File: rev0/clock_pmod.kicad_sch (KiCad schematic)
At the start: 5 parts, among them IC1 ECP5-BGA256, Y1 Osc60MHz

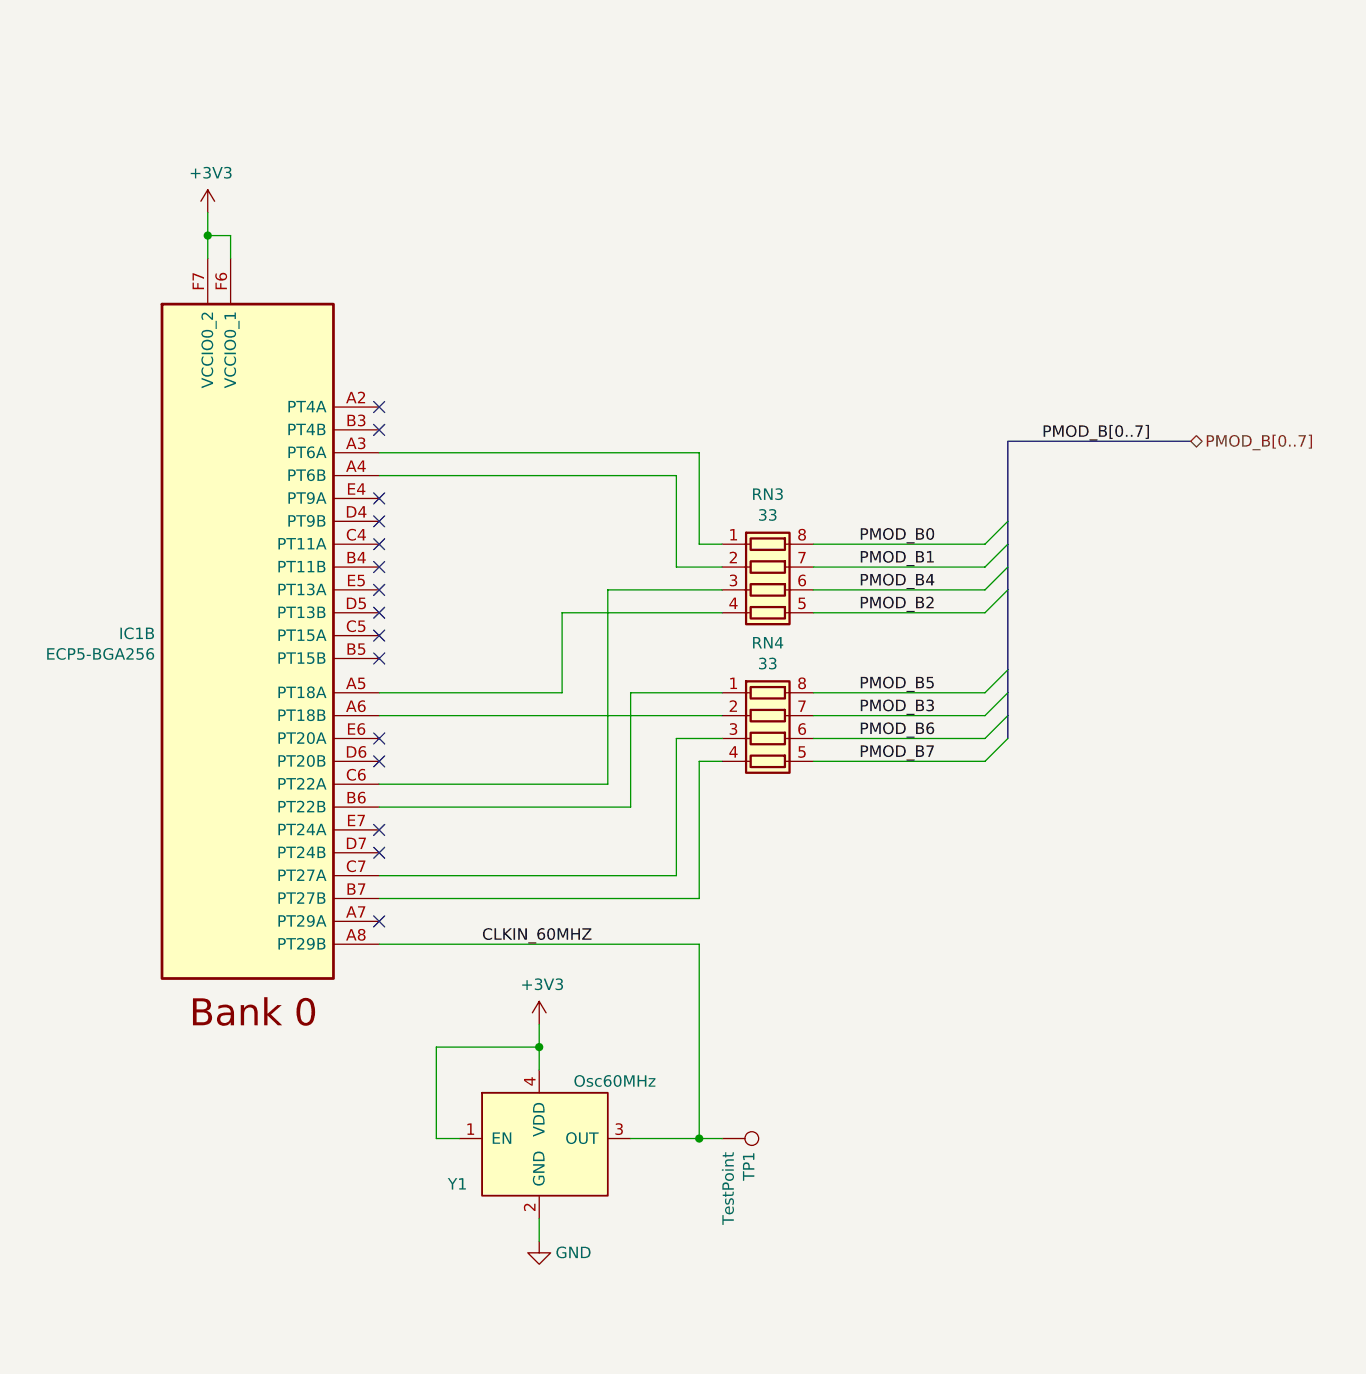
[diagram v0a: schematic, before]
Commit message: hardware: update layout to match schematic
- invert USB switch D+/D- for routing convenience
- connect *_VBUS_CLAMPED to *_VBUS_IN not *_VBUS
- reassign FPGA pins and banks for routing convenience
- connect PHY VBAT to +3V3, not +5V
- add PHY VDD33 test points
- add LED test points
- add PROGRAM button test point
- add PHY VDD33 test point
- add mezzanine connector
- improve decoupling
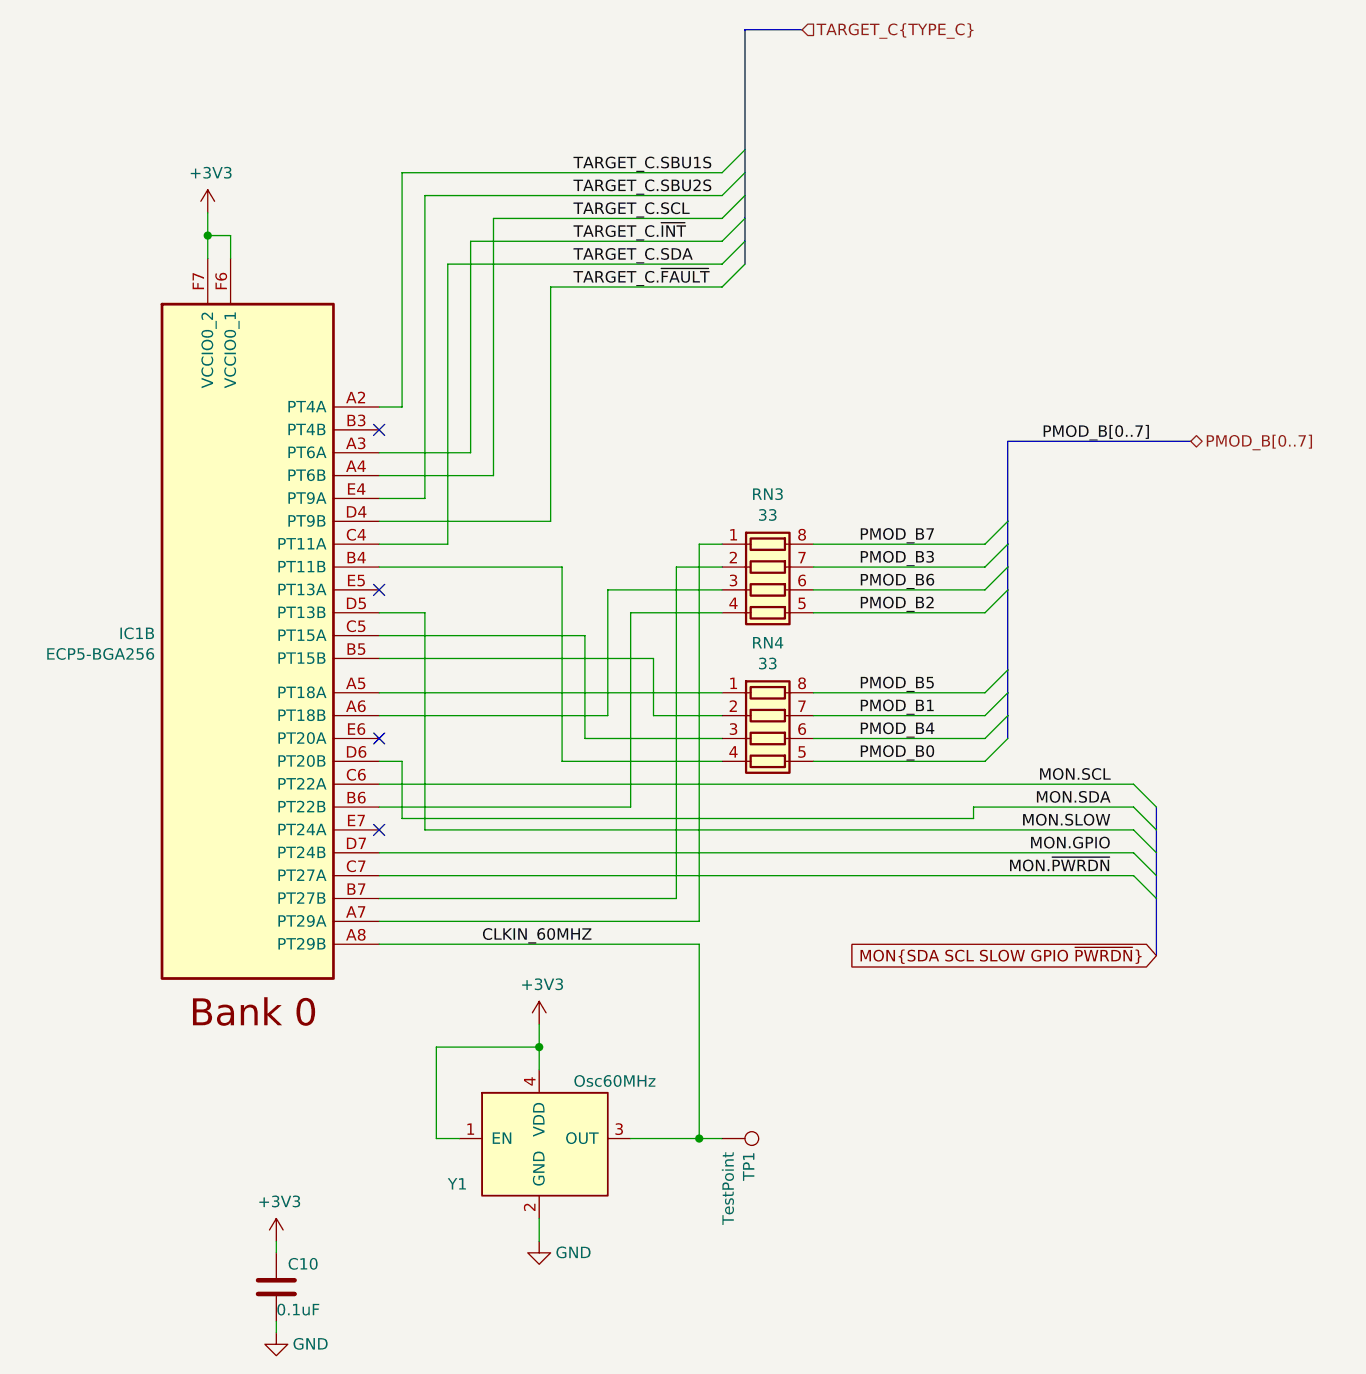
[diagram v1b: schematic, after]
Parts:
- added C10: 0.1uF, Capacitor_SMD:C_0402_1005Metric, symbol Device:C
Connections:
- net +3V3: now also C10.1
- net GND: now also C10.2
- net PMOD_B0: now also RN4.5 (R4.2); no longer RN3.8 (R1.2)
- net PMOD_B1: now also RN4.7 (R2.2); no longer RN3.7 (R2.2)
- net PMOD_B3: now also RN3.7 (R2.2); no longer RN4.7 (R2.2)
- net PMOD_B4: now also RN4.6 (R3.2); no longer RN3.6 (R3.2)
- net PMOD_B6: now also RN3.6 (R3.2); no longer RN4.6 (R3.2)
- net PMOD_B7: now also RN3.8 (R1.2); no longer RN4.5 (R4.2)
- net TARGET_C.SBU1S: now reaches IC1.A2 (PT4A)
- net at RN3.1 (R1.1): now also IC1.A7 (PT29A); no longer IC1.A3 (PT6A)
- net at RN3.2 (R2.1): now also IC1.B7 (PT27B); no longer IC1.A4 (PT6B)
- net at IC1.A5 (PT18A): now also RN4.1 (R1.1); no longer RN3.4 (R4.1)
- net at IC1.A6 (PT18B): now also RN3.3 (R3.1); no longer RN4.2 (R2.1)
- net at IC1.B4 (PT11B): now also RN4.4 (R4.1)
- net at IC1.B5 (PT15B): now also RN4.2 (R2.1)
- net at IC1.B6 (PT22B): now also RN3.4 (R4.1); no longer RN4.1 (R1.1)
- net TARGET_C.SDA: now reaches IC1.C4 (PT11A)
- net at IC1.C5 (PT15A): now also RN4.3 (R3.1)
- net MON.SCL: now reaches IC1.C6 (PT22A)
- net MON.SCL: no longer RN3.3 (R3.1)
- net MON.~{PWRDN}: now reaches IC1.C7 (PT27A)
- net MON.~{PWRDN}: no longer RN4.3 (R3.1)
- net TARGET_C.~{FAULT}: now reaches IC1.D4 (PT9B)
- net MON.SLOW: now reaches IC1.D5 (PT13B)
- net MON.SDA: now reaches IC1.D6 (PT20B)
- net MON.GPIO: now reaches IC1.D7 (PT24B)
- net TARGET_C.SBU2S: now reaches IC1.E4 (PT9A)
- new net TARGET_C.SCL: IC1.A4 (PT6B)
- new net TARGET_C.~{INT}: IC1.A3 (PT6A)
- no-connect marks 15 -> 4

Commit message: hardware: passive component selection
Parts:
- C10: Manufacturer (none) -> Samsung; Part Number GENERIC-CAP-0402-0.1uF -> CL05A104KA5NNNC
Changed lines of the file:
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@@
       (effects (font (size 1.27 1.27)) hide)
     )
-    (property "Part Number" "GENERIC-CAP-0402-0.1uF" (id 4) (at 68.58 158.75 0)
+    (property "Part Number" "CL05A104KA5NNNC" (id 4) (at 68.58 158.75 0)
       (effects (font (size 1.27 1.27)) hide)
     )
@@
       (effects (font (size 1.27 1.27)) hide)
     )
+    (property "Description" "CAP CER 0.1UF 25V X5R 0402" (id 6) (at 68.58 158.75 0)
+      (effects (font (size 1.27 1.27)) hide)
+    )
+    (property "Manufacturer" "Samsung" (id 7) (at 68.58 158.75 0)
+      (effects (font (size 1.27 1.27)) hide)
+    )
